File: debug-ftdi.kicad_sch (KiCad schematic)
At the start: 68 parts, among them J3 USB-C_GCT_USB4105-GF-A, U13 TXU0304BQAR, U5 NCP718BSN330T1G, U6 FT4232H_VQFN, U7 TXU0304BQAR, U8 TPD4E05U06QDQARQ1, U9 SN74HC595B, Y1 Resonator_12MHz_ABM8G

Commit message: [#57478] ohp release
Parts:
- C109: footprint sodimm-ddr5-tester-footprints:C_0603_1608Metric -> antmicro-footprints:C_0603_1608Metric; symbol sodimm-ddr5-tester:C_10u_25V_0603 -> antmicroCapacitors0603:C_10u_25V_0603
- C110, C112, C115, C118, C119, C120, C121, C123, C124, C125, C128, C130, C131, C133: footprint sodimm-ddr5-tester-footprints:C_0402_1005Metric -> antmicro-footprints:C_0402_1005Metric; symbol sodimm-ddr5-tester:C_100n_0402 -> antmicroCapacitors0402:C_100n_0402
- C111, C117: footprint sodimm-ddr5-tester-footprints:C_0402_1005Metric -> antmicro-footprints:C_0402_1005Metric; symbol sodimm-ddr5-tester:C_18p_0402 -> antmicroCapacitors0402:C_18p_0402
- C113: footprint sodimm-ddr5-tester-footprints:C_0402_1005Metric -> antmicro-footprints:C_0402_1005Metric; symbol sodimm-ddr5-tester:C_10u_6.3V_0402 -> antmicroCapacitors0402:C_10u_6.3V_0402
- C114, C116, C122: footprint sodimm-ddr5-tester-footprints:C_0402_1005Metric -> antmicro-footprints:C_0402_1005Metric; symbol sodimm-ddr5-tester:C_4u7_0402 -> antmicroCapacitors0402:C_4u7_0402
- D10, D11, D12, D13: footprint sodimm-ddr5-tester-footprints:LED_0603_1608Metric_G -> antmicro-footprints:LED_0603_1608Metric_G; symbol sodimm-ddr5-tester:LED_G_0603_KP-1608CGCK -> antmicroLEDIndicationDiscrete:LED_G_0603_KP-1608CGCK
- D15: footprint sodimm-ddr5-tester-footprints:SOD-523 -> antmicro-footprints:SOD-523; symbol sodimm-ddr5-tester:BAT54-02V-G3-08 -> antmicroDiodesRectifiersSingle:BAT54-02V-G3-08
- FB1, FB2: footprint sodimm-ddr5-tester-footprints:FB_0603_1608Metric -> antmicro-footprints:FB_0603_1608Metric; symbol sodimm-ddr5-tester:FB_600Z_0.5A_Murata-BLM18AG_0603 -> antmicroFerriteBeadsandChips:FB_600Z_0.5A_Murata-BLM18AG_0603
- J3: footprint sodimm-ddr5-tester-footprints:USB-C_Receptacle_GCT_USB4105-GF-A -> antmicro-footprints:USB-C_Receptacle_GCT_USB4105-GF-A; symbol sodimm-ddr5-tester:USB-C_GCT_USB4105-GF-A -> antmicroUSBConnectors:USB-C_GCT_USB4105-GF-A
- R43, R79: footprint sodimm-ddr5-tester-footprints:R_0402_1005Metric -> antmicro-footprints:R_0402_1005Metric; symbol sodimm-ddr5-tester:R_10k_0402 -> antmicroResistors0402:R_10k_0402
- R44: footprint sodimm-ddr5-tester-footprints:R_0402_1005Metric -> antmicro-footprints:R_0402_1005Metric; symbol sodimm-ddr5-tester:R_12k_0402 -> antmicroResistors0402:R_12k_0402
- R47, R48, R49, R50, R52, R53, R54, R55: footprint sodimm-ddr5-tester-footprints:R_0402_1005Metric -> antmicro-footprints:R_0402_1005Metric; symbol sodimm-ddr5-tester:R_22R_0402 -> antmicroResistors0402:R_22R_0402
- R51: footprint sodimm-ddr5-tester-footprints:R_0402_1005Metric -> antmicro-footprints:R_0402_1005Metric; symbol sodimm-ddr5-tester:R_47k_0402 -> antmicroResistors0402:R_47k_0402
- R56, R57, R58, R59, R60: footprint sodimm-ddr5-tester-footprints:R_0402_1005Metric -> antmicro-footprints:R_0402_1005Metric; symbol sodimm-ddr5-tester:R_22R_0402 -> antmicroResistors0402:R_22R_0402; now not fitted; now left out of the parts list
- R64, R65, R66, R67, R90: footprint sodimm-ddr5-tester-footprints:R_0402_1005Metric -> antmicro-footprints:R_0402_1005Metric; symbol sodimm-ddr5-tester:R_330R_0402 -> antmicroResistors0402:R_330R_0402
- R68, R69: footprint sodimm-ddr5-tester-footprints:R_0402_1005Metric -> antmicro-footprints:R_0402_1005Metric; symbol sodimm-ddr5-tester:R_5k11_0402 -> antmicroResistors0402:R_5k11_0402
- R88, R92, R93: footprint sodimm-ddr5-tester-footprints:R_0402_1005Metric -> antmicro-footprints:R_0402_1005Metric; symbol sodimm-ddr5-tester:R_0R_0402 -> antmicroResistors0402:R_0R_0402
- R91: footprint sodimm-ddr5-tester-footprints:R_0402_1005Metric -> antmicro-footprints:R_0402_1005Metric; symbol sodimm-ddr5-tester:R_0R_0402 -> antmicroResistors0402:R_0R_0402; now not fitted; now left out of the parts list
- R94, R95: footprint sodimm-ddr5-tester-footprints:R_0402_1005Metric -> antmicro-footprints:R_0402_1005Metric; symbol sodimm-ddr5-tester:R_4k7_0402 -> antmicroResistors0402:R_4k7_0402
- TP1, TP22: footprint sodimm-ddr5-tester-footprints:TP_SMD_1mm -> antmicro-footprints:TP_SMD_1mm; symbol sodimm-ddr5-tester:TP_1mm_SMD -> antmicroTestPoints:TP_1mm_SMD
- U13, U7: footprint sodimm-ddr5-tester-footprints:DHVQFN-14-1EP_2.5x3mm -> antmicro-footprints:DHVQFN-14-1EP_2.5x3mm; symbol sodimm-ddr5-tester:TXU0304BQAR -> antmicroLogicTranslatorsLevelShifters:TXU0304BQAR
- U5: footprint sodimm-ddr5-tester-footprints:SOT-23-5 -> antmicro-footprints:SOT-23-5; symbol sodimm-ddr5-tester:NCP718BSN330T1G -> antmicroPMICVoltageRegulatorsLinear:NCP718BSN330T1G
- U6: footprint sodimm-ddr5-tester-footprints:QFN-56-1EP_8x8mm_P0.5mm -> antmicro-footprints:QFN-56-1EP_8x8mm_P0.5mm; symbol sodimm-ddr5-tester:FT4232H_VQFN -> antmicroInterfaceControllers:FT4232H_VQFN
- U8: footprint sodimm-ddr5-tester-footprints:USON-10_2.5x1mm_P0.5mm -> antmicro-footprints:USON-10_2.5x1mm_P0.5mm; symbol sodimm-ddr5-tester:TPD4E05U06QDQARQ1 -> antmicroTVSDiodes:TPD4E05U06QDQARQ1
- U9: footprint sodimm-ddr5-tester-footprints:X1QFN-16-1EP_2.5x2.5mm -> antmicro-footprints:X1QFN-16-1EP_2.5x2.5mm; symbol sodimm-ddr5-tester:SN74HC595B -> antmicroLogicShiftRegisters:SN74HC595B
- Y1: footprint sodimm-ddr5-tester-footprints:Oscillator_SMD_Geyer_KX-7-4Pin_3.2x2.5mm -> antmicro-footprints:Resonator_SMD_Abracon_ABM8G_3.2x2.5mm; symbol sodimm-ddr5-tester:Resonator_12MHz_ABM8G -> antmicroResonators:Resonator_12MHz_ABM8G

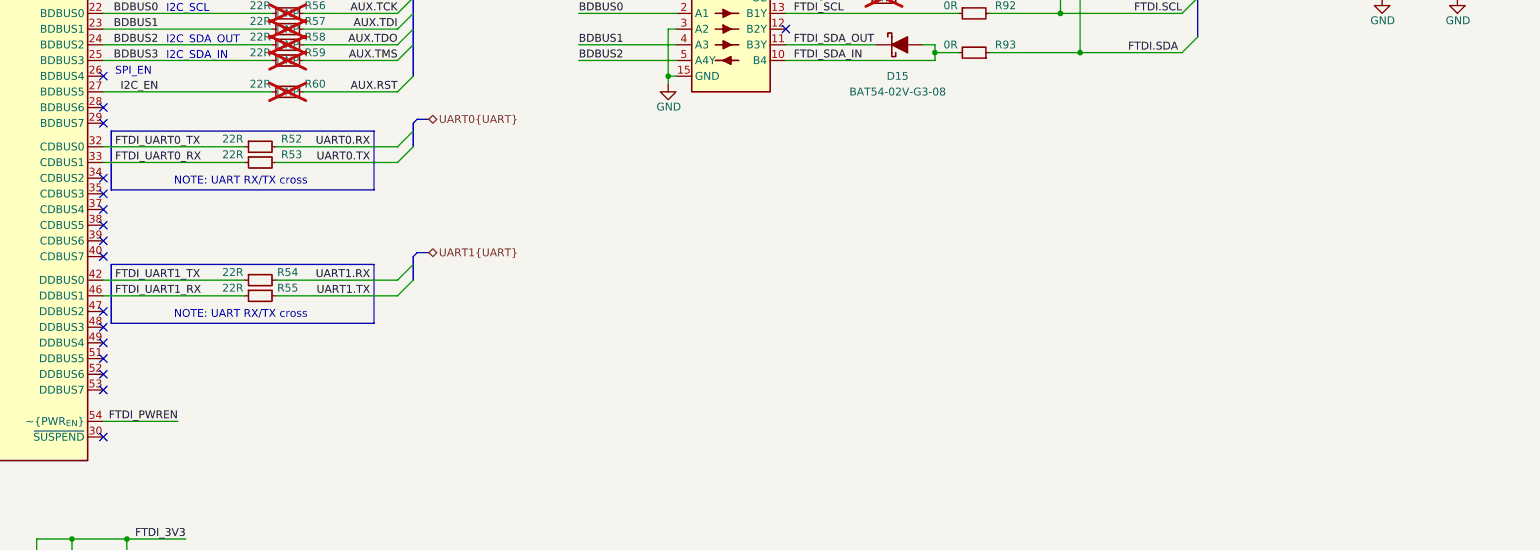
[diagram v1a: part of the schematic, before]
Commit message: [#58418] Update obsolete MPNs. Replace fuses. Remap PWR_EN and PWR_GOOD. Add UART logic level conventers. Bump revision to 1.2.0
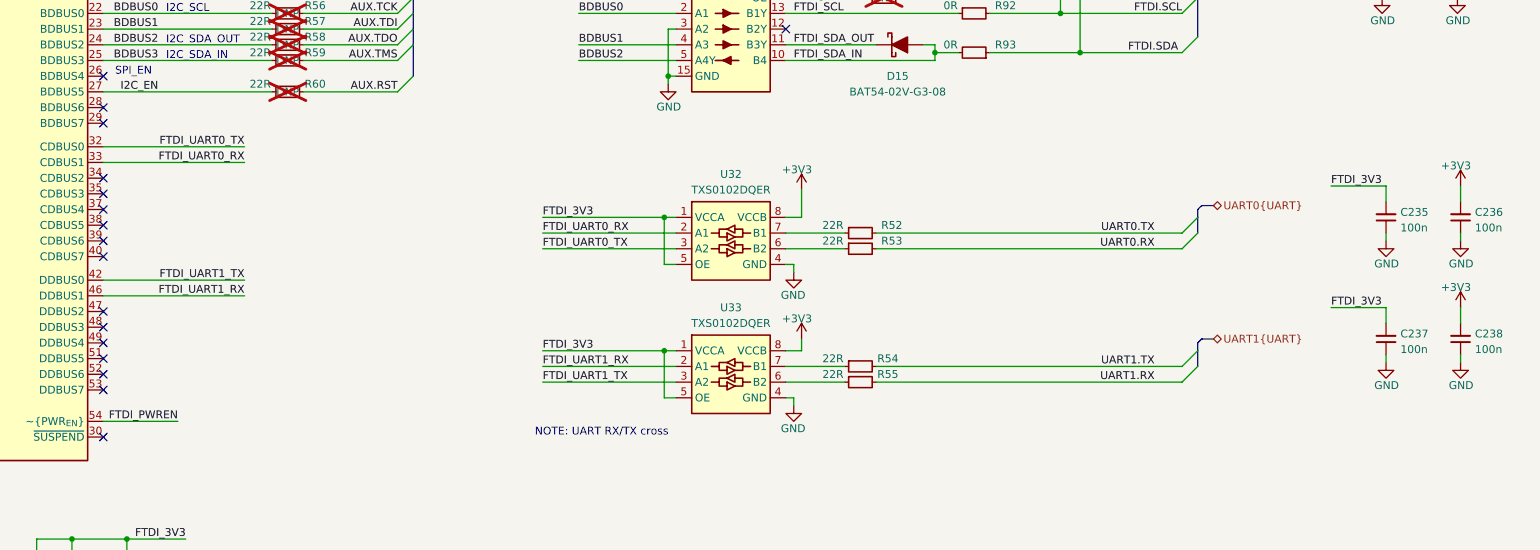
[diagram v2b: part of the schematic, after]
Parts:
- added C235, C236, C237, C238: C_100n_0402, antmicro-footprints:C_0402_1005Metric, symbol antmicroCapacitors0402:C_100n_0402
- added U32, U33: TXS0102DQER, antmicro-footprints:X2SON8_1.4x1x0.32mm_P0.35mm, symbol antmicroLogicTranslatorsLevelShifters:TXS0102DQER
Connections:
- net +3V3: now also C236.2, C238.2, U32.8 (VCCB), U33.8 (VCCB)
- net FTDI_3V3: now also C235.2, C237.2, U32.1 (VCCA), U32.5 (OE), U33.1 (VCCA), U33.5 (OE)
- net FTDI_UART0_RX: now also U32.2 (A1); no longer R53.1
- net FTDI_UART0_TX: now also U32.3 (A2); no longer R52.1
- net FTDI_UART1_RX: now also U33.2 (A1); no longer R55.1
- net FTDI_UART1_TX: now also U33.3 (A2); no longer R54.1
- net GND: now also C235.1, C236.1, C237.1, C238.1, U32.4 (GND), U33.4 (GND)
- net UART0.RX: now also R53.2; no longer R52.2
- net UART0.TX: now also R52.2; no longer R53.2
- net UART1.RX: now also R55.2; no longer R54.2
- net UART1.TX: now also R54.2; no longer R55.2
- new net: R52.1, U32.7 (B1)
- new net: R55.1, U33.6 (B2)
- new net: R53.1, U32.6 (B2)
- new net: R54.1, U33.7 (B1)
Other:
- moved on the sheet: R52, R53, R54, R55

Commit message: [#86301] Project refresh 81589
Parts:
- R56, R57, R58, R59, R60, R91: DNP DNP -> (none)

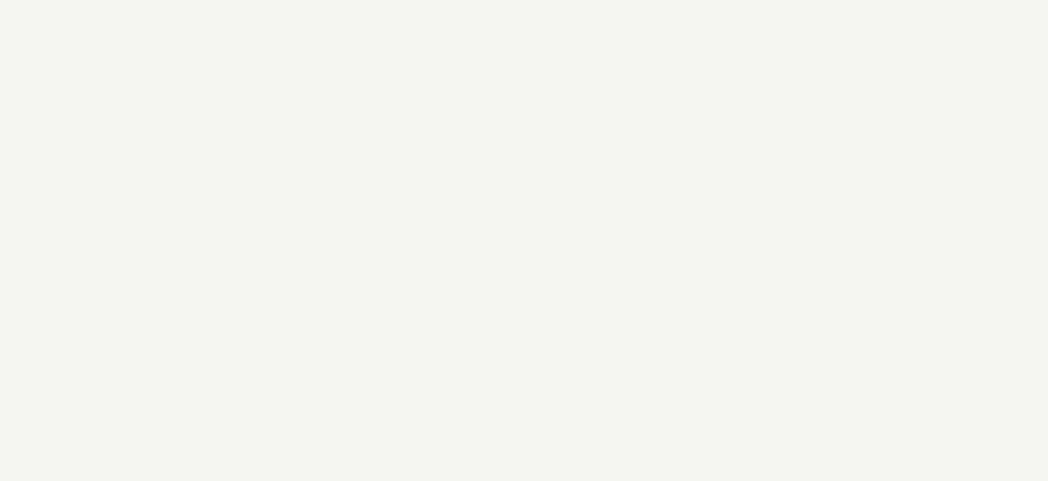
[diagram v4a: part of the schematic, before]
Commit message: [#87036] Add IC testpoints
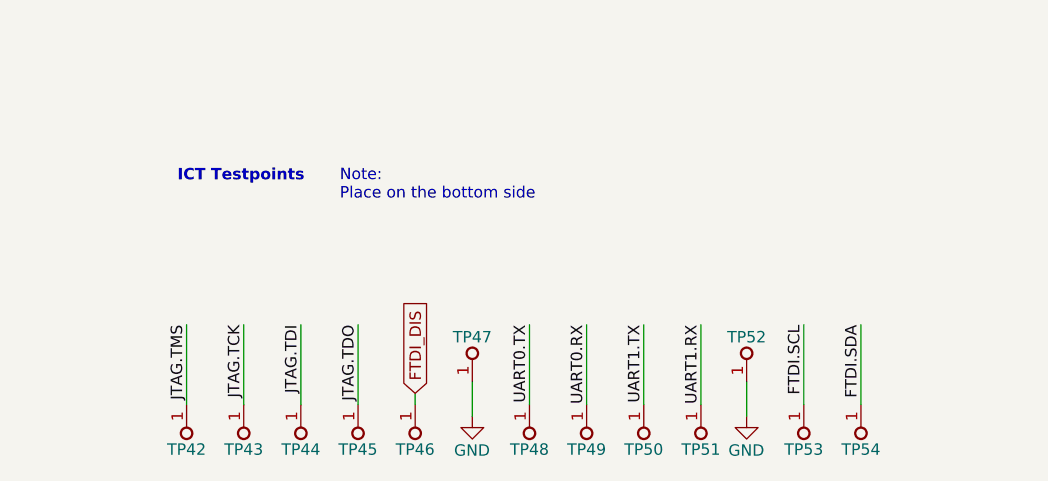
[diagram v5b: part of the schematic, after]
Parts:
- added TP42, TP43, TP44, TP45, TP46, TP47, TP48, TP49, TP50, TP51, TP52, TP53, TP54: TP_1mm_SMD, antmicro-footprints:TP_SMD_1mm, symbol antmicroTestPoints:TP_1mm_SMD
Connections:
- net FTDI.SCL: now also TP53.1
- net FTDI.SDA: now also TP54.1
- net FTDI_DIS: now also TP46.1
- net GND: now also TP47.1, TP52.1
- net JTAG.TCK: now also TP43.1
- net JTAG.TDI: now also TP44.1
- net JTAG.TDO: now also TP45.1
- net JTAG.TMS: now also TP42.1
- net UART0.RX: now also TP49.1
- net UART0.TX: now also TP48.1
- net UART1.RX: now also TP51.1
- net UART1.TX: now also TP50.1
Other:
- note added: "ICT Testpoints"
- note added: "Note: Place on the bottom side"

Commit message: [#87036] Update D15
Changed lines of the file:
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@@
 	(wire
 		(pts
+			(xy 284.48 143.51) (xy 287.02 143.51)
+		)
+		(stroke
+			(width 0)
+			(type default)
+		)
+	)
+	(wire
+		(pts
 			(xy 68.58 239.395) (xy 68.58 245.745)
 		)
@@
 	(wire
 		(pts
-			(xy 285.115 143.51) (xy 287.02 143.51)
-		)
-		(stroke
-			(width 0)
-			(type default)
-		)
-	)
-	(wire
-		(pts
 			(xy 277.495 107.315) (xy 327.025 107.315)
 		)
@@
 	(wire
 		(pts
-			(xy 262.89 143.51) (xy 277.495 143.51)
+			(xy 262.89 143.51) (xy 279.4 143.51)
 		)
 		(stroke
@@
 	)
 	(symbol
-		(lib_id "antmicropower:GND")
-		(at 361.315 111.125 0)
+		(lib_name "BAT54-02V-G3-08_1")
+		(lib_id "antmicroDiodesRectifiersSingle:BAT54-02V-G3-08")
+		(at 279.4 143.51 0)
 		(unit 1)
 		(exclude_from_sim no)
@@
 		(on_board yes)
 		(dnp no)
-		(property "Reference" "#PWR0196"
-			(at 361.315 117.475 0)
+		(property "Reference" "D15"
+			(at 281.94 147.32 0)
 			(effects
 				(font
 					(size 1.27 1.27)
+					(thickness 0.15)
 				)
-				(hide yes)
 			)
 		)
-		(property "Value" "GND"
-			(at 359.41 115.57 0)
+		(property "Value" "BAT54-02V-G3-08"
+			(at 300.99 158.75 0)
 			(effects
 				(font
@@
 				)
 				(justify left bottom)
+				(hide yes)
 			)
 		)
-		(property "Footprint" ""
-			(at 370.205 118.745 0)
+		(property "Footprint" "antmicro-footprints:SOD-523"
+			(at 300.99 153.67 0)
 			(effects
 				(font
@@
 			)
 		)
-		(property "Datasheet" ""
-			(at 370.205 123.825 0)
+		(property "Datasheet" "https://www.vishay.com/docs/85633/bat5402v.pdf"
+			(at 300.99 156.21 0)
 			(effects
 				(font
@@
 			)
 		)
-		(property "Description" ""
-			(at 370.205 126.365 0)
+		(property "Description" "Small Signal Schottky Diode, Single, 30 V, 200 mA, 800 mV, 600 mA, 125 °C"
+			(at 300.99 168.91 0)
 			(effects
 				(font
@@
 			)
 		)
+		(property "MPN" "BAT54-02V-G3-08"
+			(at 281.94 149.352 0)
+			(effects
+				(font
+					(size 1.27 1.27)
+					(thickness 0.15)
+				)
+			)
+		)
+		(property "Manufacturer" "Vishay"
+			(at 300.99 161.29 0)
+			(effects
+				(font
+					(size 1.27 1.27)
+					(thickness 0.15)
+				)
+				(justify left bottom)
+				(hide yes)
+			)
+		)
 		(property "Author" "Antmicro"
-			(at 370.205 118.745 0)
+			(at 300.99 163.83 0)
 			(effects
 				(font
@@
 		)
 		(property "License" "Apache-2.0"
-			(at 370.205 121.285 0)
+			(at 300.99 166.37 0)
 			(effects
 				(font
@@
 			)
 		)
+		(pin "2"
+		)
 		(pin "1"
 		)
 		(instances
-			(project "sodimm-ddr5-tester"
+			(project ""
 				(path "/1faa6543-e26a-4449-8bac-ee14b9f19e5f/00000000-0000-0000-0000-0000600e76d8"
-					(reference "#PWR0196")
+					(reference "D15")
 					(unit 1)
 				)
@@
 	(symbol
 		(lib_id "antmicropower:GND")
-		(at 58.547 147.32 0)
+		(at 361.315 111.125 0)
 		(unit 1)
 		(exclude_from_sim no)
@@
 		(on_board yes)
 		(dnp no)
-		(fields_autoplaced yes)
-		(property "Reference" "#PWR0257"
-			(at 58.547 153.67 0)
+		(property "Reference" "#PWR0196"
+			(at 361.315 117.475 0)
 			(effects
 				(font
@@
 		)
 		(property "Value" "GND"
-			(at 60.96 148.59 0)
+			(at 359.41 115.57 0)
 			(effects
 				(font
@@
 					(thickness 0.15)
 				)
-				(justify left)
+				(justify left bottom)
 			)
 		)
 		(property "Footprint" ""
-			(at 67.437 154.94 0)
+			(at 370.205 118.745 0)
 			(effects
 				(font
@@
 		)
 		(property "Datasheet" ""
-			(at 67.437 160.02 0)
+			(at 370.205 123.825 0)
 			(effects
 				(font
@@
 		)
 		(property "Description" ""
-			(at 67.437 162.56 0)
+			(at 370.205 126.365 0)
 			(effects
 				(font
@@
 		)
 		(property "Author" "Antmicro"
-			(at 67.437 154.94 0)
+			(at 370.205 118.745 0)
 			(effects
 				(font
@@
 		)
 		(property "License" "Apache-2.0"
-			(at 67.437 157.48 0)
+			(at 370.205 121.285 0)
 			(effects
 				(font
@@
 			(project "sodimm-ddr5-tester"
 				(path "/1faa6543-e26a-4449-8bac-ee14b9f19e5f/00000000-0000-0000-0000-0000600e76d8"
-					(reference "#PWR0257")
+					(reference "#PWR0196")
 					(unit 1)
 				)
@@
 	)
 	(symbol
-		(lib_id "antmicroDiodesRectifiersSingle:BAT54-02V-G3-08")
-		(at 285.115 143.51 180)
+		(lib_id "antmicropower:GND")
+		(at 58.547 147.32 0)
 		(unit 1)
 		(exclude_from_sim no)
@@
 		(dnp no)
 		(fields_autoplaced yes)
-		(property "Reference" "D15"
-			(at 280.9875 148.59 0)
+		(property "Reference" "#PWR0257"
+			(at 58.547 153.67 0)
 			(effects
 				(font
 					(size 1.27 1.27)
 				)
+				(hide yes)
 			)
 		)
-		(property "Value" "BAT54-02V-G3-08"
-			(at 280.9875 151.13 0)
+		(property "Value" "GND"
+			(at 60.96 148.59 0)
 			(effects
 				(font
@@
 					(thickness 0.15)
 				)
+				(justify left)
 			)
 		)
-		(property "Footprint" "antmicro-footprints:SOD-523"
-			(at 263.525 133.35 0)
+		(property "Footprint" ""
+			(at 67.437 154.94 0)
 			(effects
 				(font
@@
 			)
 		)
-		(property "Datasheet" "https://www.mouser.com/datasheet/2/427/bat5402v-2897987.pdf"
-			(at 263.525 130.81 0)
+		(property "Datasheet" ""
+			(at 67.437 160.02 0)
 			(effects
 				(font
@@
 		)
 		(property "Description" ""
-			(at 285.115 143.51 0)
-			(effects
-				(font
-					(size 1.27 1.27)
-				)
-			)
-		)
-		(property "MPN" "BAT54-02V-G3-08"
-			(at 263.525 128.27 0)
-			(effects
-				(font
-					(size 1.27 1.27)
-					(thickness 0.15)
-				)
-				(justify left bottom)
-				(hide yes)
-			)
-		)
-		(property "Manufacturer" "Vishay"
-			(at 263.525 125.73 0)
+			(at 67.437 162.56 0)
 			(effects
 				(font
 					(size 1.27 1.27)
-					(thickness 0.15)
 				)
 				(justify left bottom)
@@
 		)
 		(property "Author" "Antmicro"
-			(at 263.525 123.19 0)
+			(at 67.437 154.94 0)
 			(effects
 				(font
@@
 		)
 		(property "License" "Apache-2.0"
-			(at 263.525 120.65 0)
+			(at 67.437 157.48 0)
 			(effects
 				(font
@@
 		(pin "1"
 		)
-		(pin "2"
-		)
 		(instances
 			(project "sodimm-ddr5-tester"
 				(path "/1faa6543-e26a-4449-8bac-ee14b9f19e5f/00000000-0000-0000-0000-0000600e76d8"
-					(reference "D15")
+					(reference "#PWR0257")
 					(unit 1)
 				)
